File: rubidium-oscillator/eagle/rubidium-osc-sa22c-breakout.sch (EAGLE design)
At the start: 13 parts, among them J1 OSC_TMMH-109-01-G-DV-ES-A, Q1 ZXMP10A13F, Q2 ZXMP10A13F, X1 MKDSN4, X2 MPT3, X3 MPT6, X4 SMA-142-0701-801/806, X5 SMA-142-0701-801/806, X6 SMA-142-0701-801/806

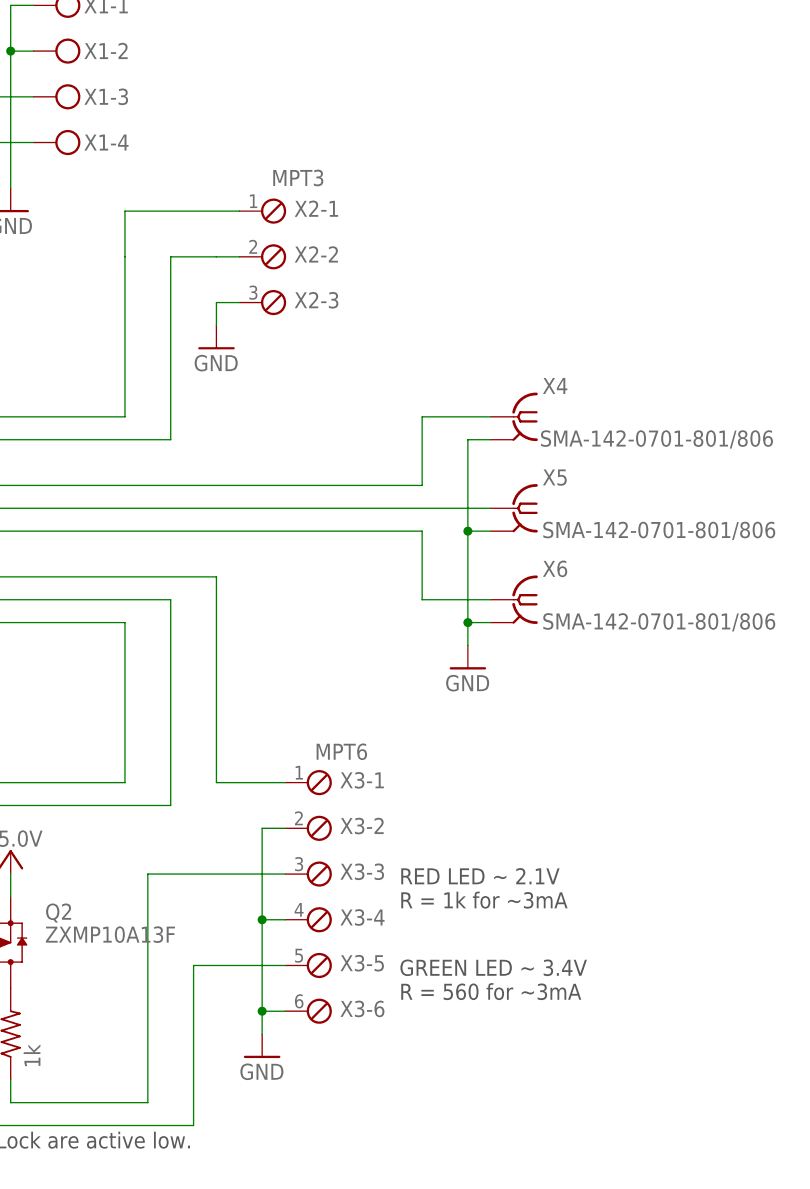
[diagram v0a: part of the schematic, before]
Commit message: Revamped layout
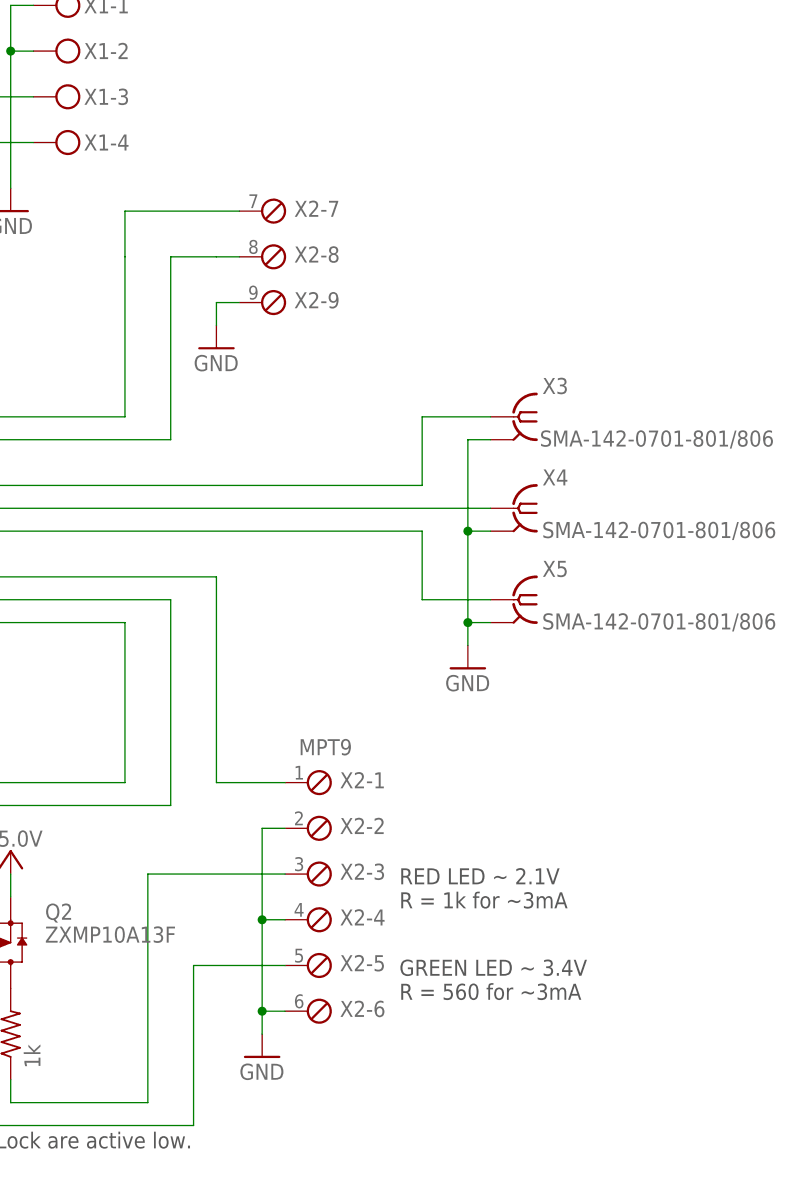
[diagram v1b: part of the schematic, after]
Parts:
- removed X6: SMA-142-0701-801/806, con-coax:SMA-142-0701-801/806
- X2: value MPT3 -> MPT9; device con-phoenix-254:MPT3 -> con-phoenix-254:MPT9
- X3: value MPT6 -> SMA-142-0701-801/806; device con-phoenix-254:MPT6 -> con-coax:SMA-142-0701-801/806
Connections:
- net GND: now also X2-2.1, X2-4.1, X2-6.1, X2-9.1, X3.2; no longer X2-3.1, X3-2.1, X3-4.1, X3-6.1, X6.2
- net N$1: now also X3.1; no longer X4.1
- net N$12: now also X2-3.1; no longer X3-3.1
- net N$13: now also X2-5.1; no longer X3-5.1
- net N$2: now also X4.1; no longer X5.1
- net N$3: now also X5.1; no longer X6.1
- net N$4: now also X2-7.1; no longer X2-1.1
- net N$5: now also X2-8.1; no longer X2-2.1
- net N$7: now also X2-1.1; no longer X3-1.1
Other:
- moved on the sheet: X2-1, X2-2, X2-3, X4, X5

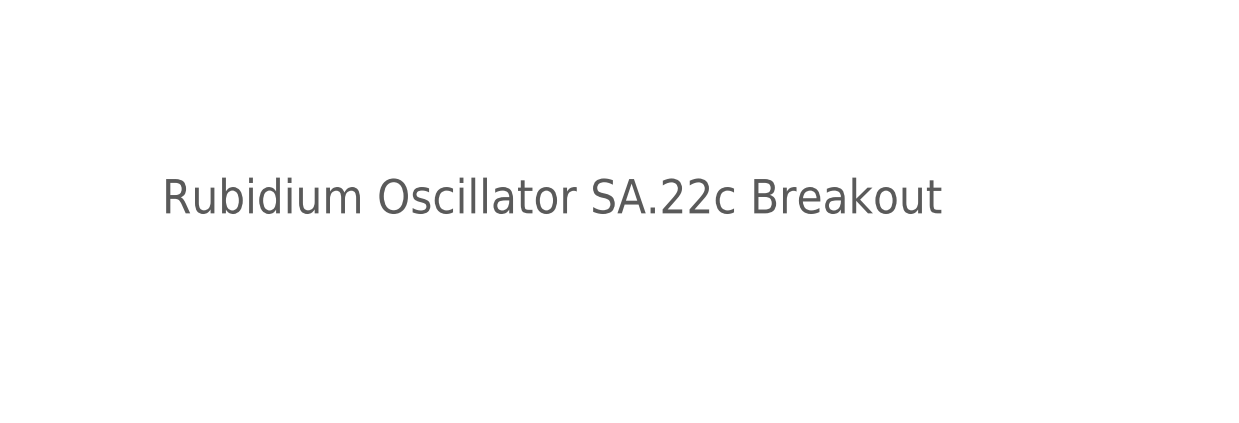
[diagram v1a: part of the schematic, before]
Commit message: Adjust for proper Phoenix conn sizes.
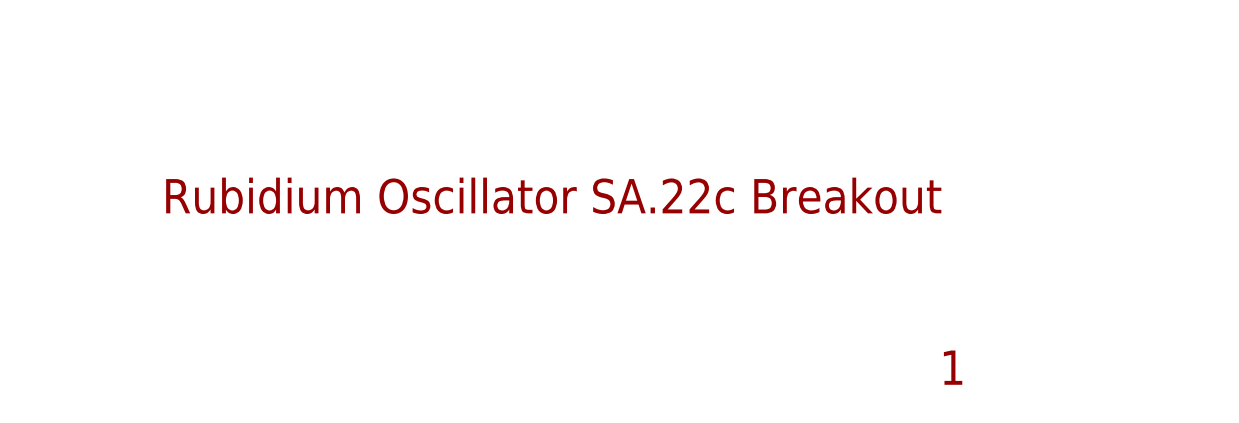
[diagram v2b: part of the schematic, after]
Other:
- note added: "1"
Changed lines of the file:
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@@
 <setting verticaltext="up"/>
 </settings>
-<grid distance="0.05" unitdist="inch" unit="inch" style="lines" multiple="2" display="yes" altdistance="0.01" altunitdist="inch" altunit="inch"/>
+<grid distance="0.1" unitdist="inch" unit="inch" style="lines" multiple="1" display="no" altdistance="0.01" altunitdist="inch" altunit="inch"/>
 <layers>
 <layer number="1" name="Top" color="4" fill="1" visible="no" active="no"/>
@@
 <sheet>
 <plain>
-<text x="177.8" y="25.4" size="3.81" layer="97">Rubidium Oscillator SA.22c Breakout</text>
+<text x="177.8" y="25.4" size="3.81" layer="94">Rubidium Oscillator SA.22c Breakout</text>
 <text x="157.48" y="64.77" size="1.778" layer="97">GREEN LED ~ 3.4V
 R = 560 for ~3mA</text>
@@
 R = 1k for ~3mA</text>
 <text x="91.44" y="48.26" size="1.778" layer="97">NOTE: Service and Lock are active low.</text>
+<text x="264.16" y="6.35" size="3.81" layer="94">1</text>
 </plain>
 <instances>

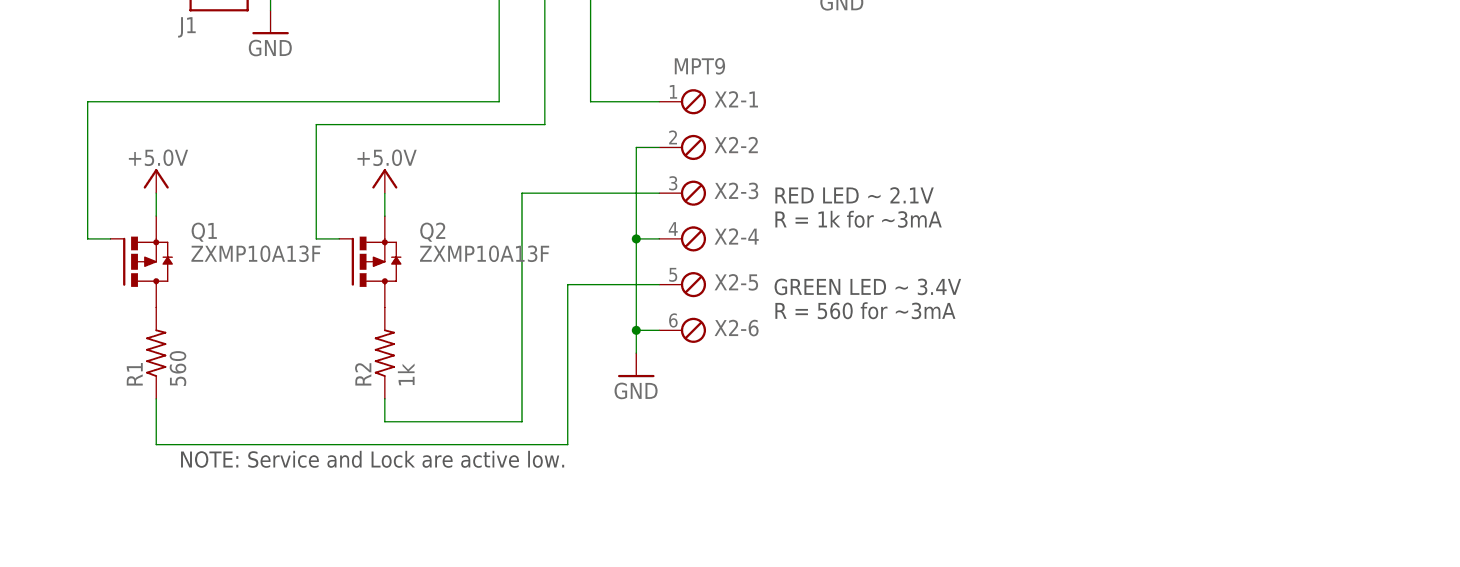
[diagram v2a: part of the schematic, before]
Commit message: Update vias to tented and moved some, change R1 and R2 for 10mA LEDs
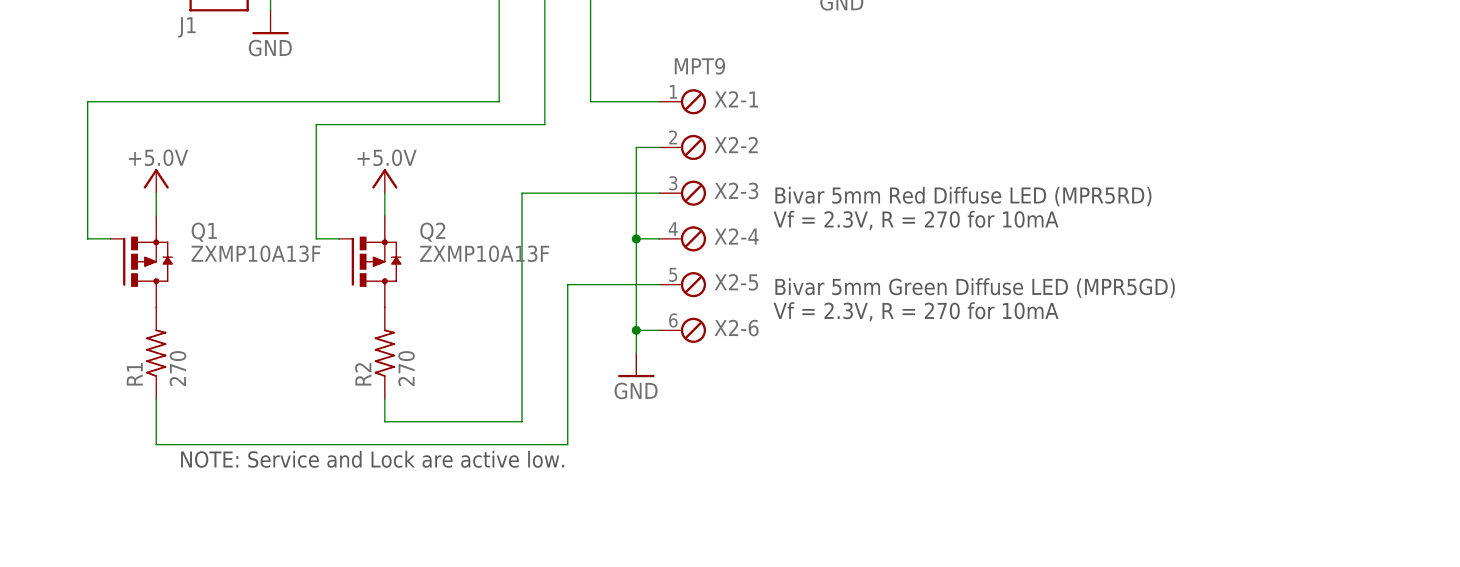
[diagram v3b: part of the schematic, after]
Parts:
- R1: value 560 -> 270
- R2: value 1k -> 270
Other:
- note added: "Bivar 5mm Green Diffuse LED (MPR5GD) Vf = 2.3V, R = 270 for 10mA"
- note added: "Bivar 5mm Red Diffuse LED (MPR5RD) Vf = 2.3V, R = 270 for 10mA"
- note removed: "GREEN LED ~ 3.4V R = 560 for ~3mA"
- note removed: "RED LED ~ 2.1V R = 1k for ~3mA"
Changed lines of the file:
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@@
 <part name="GND5" library="supply1" library_urn="urn:adsk.eagle:library:371" deviceset="GND" device=""/>
 <part name="Q1" library="transistor-power" library_urn="urn:adsk.eagle:library:400" deviceset="FDN360P" device="" package3d_urn="urn:adsk.eagle:package:29529/2" value="ZXMP10A13F"/>
-<part name="R1" library="rcl" library_urn="urn:adsk.eagle:library:334" deviceset="R-US_" device="R0603" package3d_urn="urn:adsk.eagle:package:23555/3" value="560"/>
+<part name="R1" library="rcl" library_urn="urn:adsk.eagle:library:334" deviceset="R-US_" device="R0603" package3d_urn="urn:adsk.eagle:package:23555/3" value="270"/>
 <part name="Q2" library="transistor-power" library_urn="urn:adsk.eagle:library:400" deviceset="FDN360P" device="" package3d_urn="urn:adsk.eagle:package:29529/2" value="ZXMP10A13F"/>
-<part name="R2" library="rcl" library_urn="urn:adsk.eagle:library:334" deviceset="R-US_" device="R0603" package3d_urn="urn:adsk.eagle:package:23555/3" value="1k"/>
+<part name="R2" library="rcl" library_urn="urn:adsk.eagle:library:334" deviceset="R-US_" device="R0603" package3d_urn="urn:adsk.eagle:package:23555/3" value="270"/>
 <part name="C1" library="rcl" library_urn="urn:adsk.eagle:library:334" deviceset="C-EU" device="C0603" package3d_urn="urn:adsk.eagle:package:23616/2" value="100n"/>
 <part name="C2" library="rcl" library_urn="urn:adsk.eagle:library:334" deviceset="C-EU" device="C0603" package3d_urn="urn:adsk.eagle:package:23616/2" value="100n"/>
@@
 <plain>
 <text x="177.8" y="25.4" size="3.81" layer="94">Rubidium Oscillator SA.22c Breakout</text>
-<text x="157.48" y="64.77" size="1.778" layer="97">GREEN LED ~ 3.4V
-R = 560 for ~3mA</text>
-<text x="157.48" y="74.93" size="1.778" layer="97">RED LED ~ 2.1V
-R = 1k for ~3mA</text>
+<text x="157.48" y="64.77" size="1.778" layer="97">Bivar 5mm Green Diffuse LED (MPR5GD)
+Vf = 2.3V, R = 270 for 10mA</text>
+<text x="157.48" y="74.93" size="1.778" layer="97">Bivar 5mm Red Diffuse LED (MPR5RD)
+Vf = 2.3V, R = 270 for 10mA</text>
 <text x="91.44" y="48.26" size="1.778" layer="97">NOTE: Service and Lock are active low.</text>
 <text x="264.16" y="6.35" size="3.81" layer="94">1</text>
